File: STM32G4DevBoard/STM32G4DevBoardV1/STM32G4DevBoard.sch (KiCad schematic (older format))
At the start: 26 parts, among them J1 USB_B_Micro, J2 Conn_01x13, J3 Conn_01x13, U1 STM32G431KBTx, U2 LD3985M33R_SOT23, Y1 24MHz

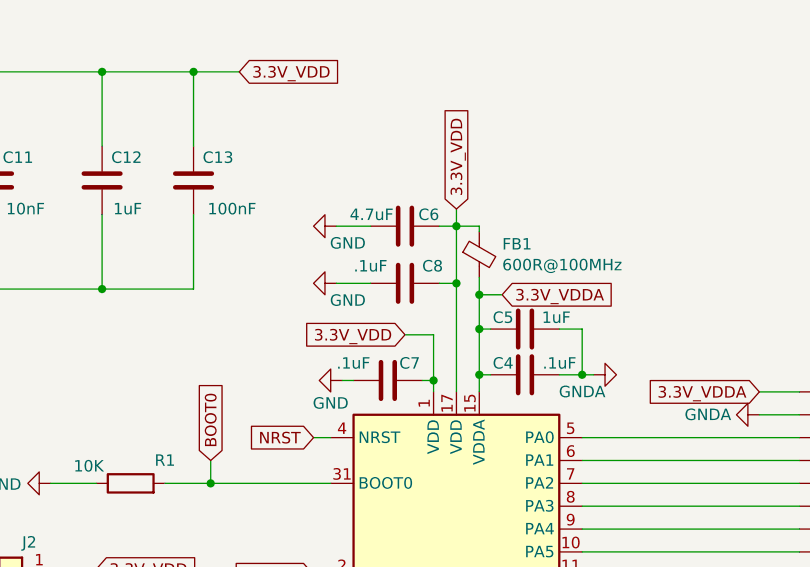
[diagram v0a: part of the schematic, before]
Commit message: Made plenty of Progress, finish routing power and a couple of pins
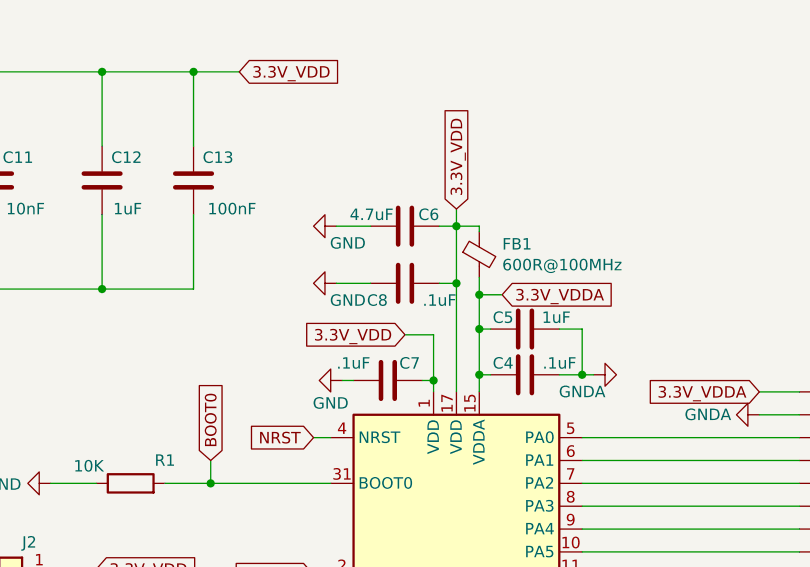
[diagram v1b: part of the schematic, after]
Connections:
- net 3.3V_VDD: now also C8.2; no longer C8.1
- net GND: now also C8.1; no longer C8.2
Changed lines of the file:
@@
 	6450 2900 6450 3100
-Wire Wire Line
-	6175 2675 6025 2675
 Wire Wire Line
 	6550 2675 6550 3150
@@
 F 3 "~" H 6325 2675 50  0001 C CNN
 	1    6325 2675
-	0    1    1    0
+	0    -1   -1   0
 $EndComp
 Wire Wire Line
@@
 Wire Wire Line
 	8050 4350 7900 4350
+Wire Wire Line
+	6175 2675 6025 2675
 $EndSCHEMATC

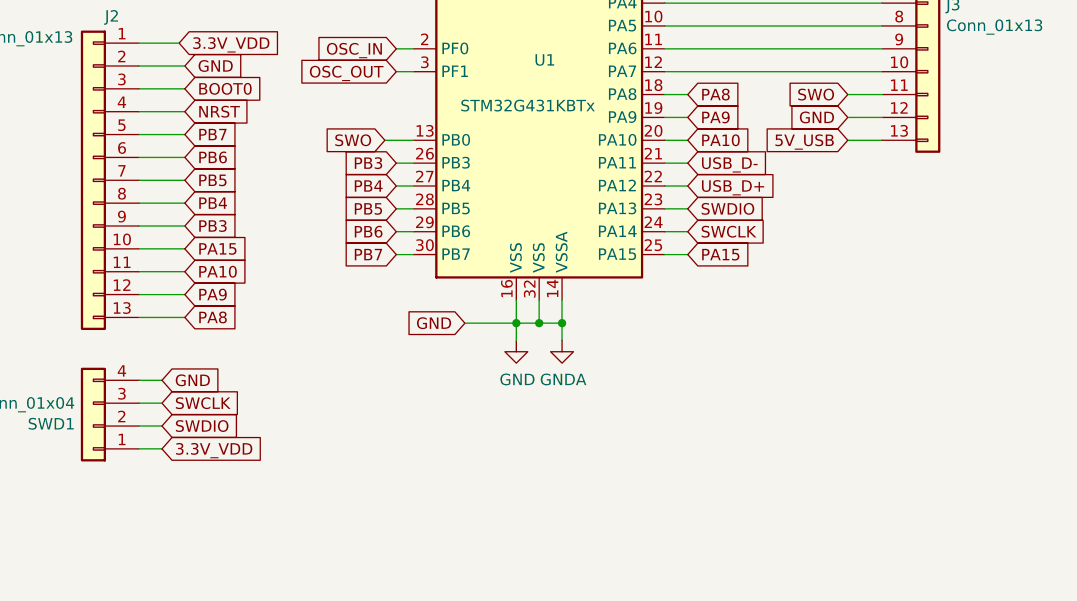
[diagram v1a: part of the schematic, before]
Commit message: Finish Power splitting and pin routing
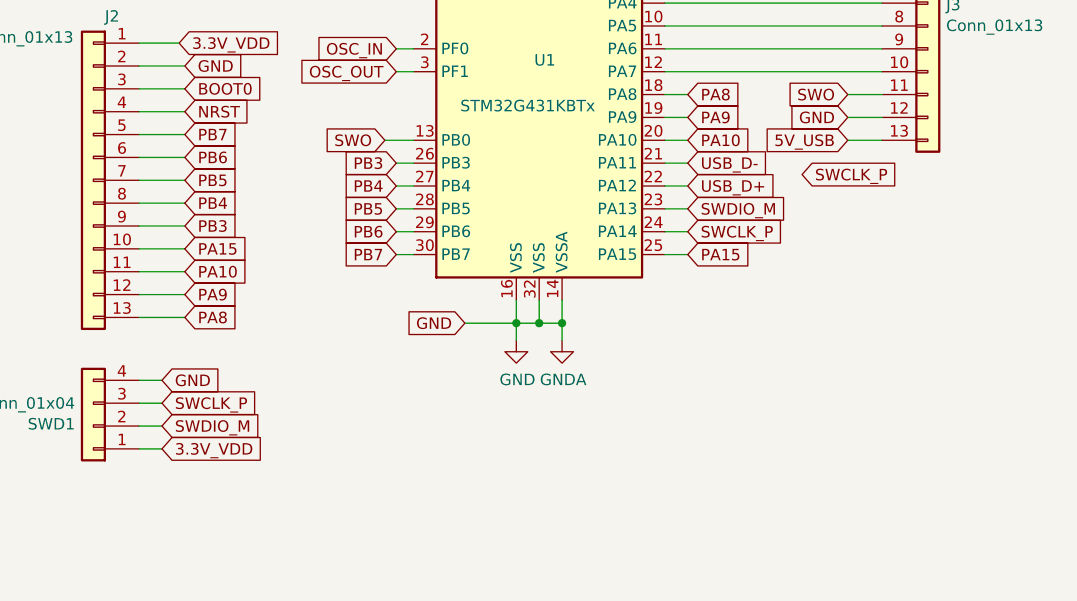
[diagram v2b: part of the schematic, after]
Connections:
- net SWCLK renamed SWCLK_P
- net SWDIO renamed SWDIO_M
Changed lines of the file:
@@
 Wire Wire Line
 	4800 5400 4900 5400
-Text GLabel 4900 5600 2    50   Input ~ 0
-SWDIO
 Wire Wire Line
 	4800 5600 4900 5600
-Text GLabel 4900 5500 2    50   Input ~ 0
-SWCLK
 Wire Wire Line
 	4900 5500 4800 5500
 Wire Wire Line
 	7200 4750 7100 4750
-Text GLabel 7200 4750 2    50   Input ~ 0
-SWCLK
 Wire Wire Line
 	7200 4650 7100 4650
-Text GLabel 7200 4650 2    50   Input ~ 0
-SWDIO
 Wire Wire Line
 	6450 5150 6225 5150
@@
 Wire Wire Line
 	6175 2675 6025 2675
+Text GLabel 4900 5500 2    50   Input ~ 0
+SWCLK_P
+Text GLabel 4900 5600 2    50   Input ~ 0
+SWDIO_M
+Text GLabel 7700 4500 2    50   Input ~ 0
+SWCLK_P
+Text GLabel 7200 4750 2    50   Input ~ 0
+SWCLK_P
+Text GLabel 7200 4650 2    50   Input ~ 0
+SWDIO_M
 $EndSCHEMATC

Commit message: Completed splitting ground plane and board routing
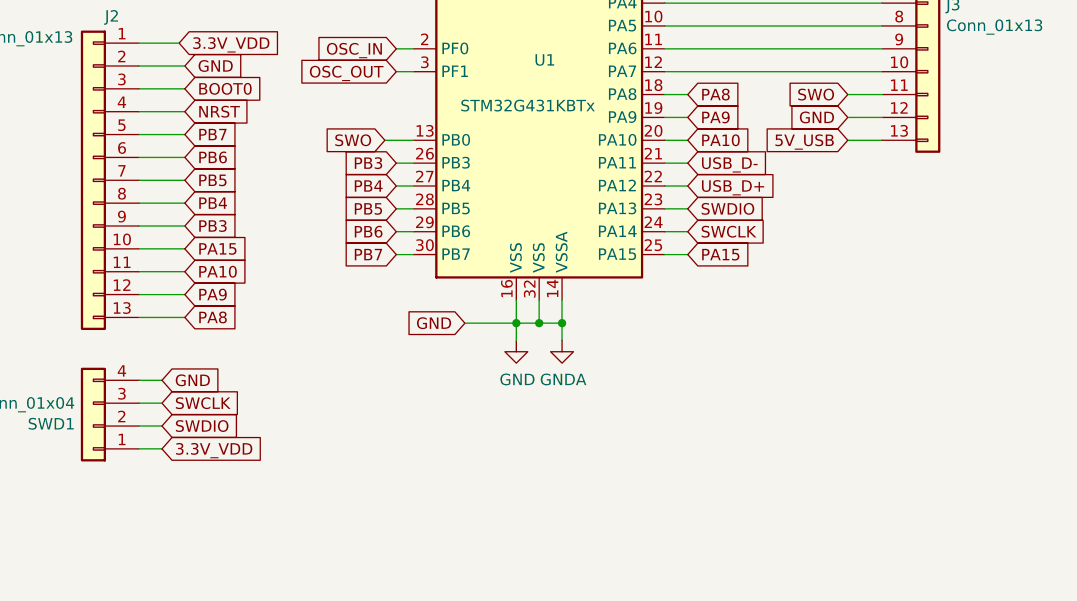
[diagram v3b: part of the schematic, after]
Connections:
- net SWCLK_P renamed SWCLK
- net SWDIO_M renamed SWDIO
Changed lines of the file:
@@
 Text GLabel 4900 5700 2    50   Input ~ 0
 3.3V_VDD
-Text GLabel 4900 5400 2    50   Input ~ 0
-GND
 Wire Wire Line
 	6650 2725 6650 2875
@@
 Text GLabel 7900 4350 0    50   Input ~ 0
 5V_USB
-Text GLabel 7900 4250 0    50   Input ~ 0
-GND
 Text GLabel 7200 4550 2    50   Input ~ 0
 USB_D+
@@
 	5000 5125 4800 5125
 Wire Wire Line
-	8050 4250 7900 4250
-Wire Wire Line
 	8050 3250 7875 3250
 Wire Wire Line
 	8050 3150 7875 3150
-Wire Wire Line
-	5000 4025 4800 4025
 Wire Wire Line
 	7100 4350 7200 4350
@@
 Wire Wire Line
 	5000 4125 4800 4125
-Text GLabel 5000 4025 2    50   Input ~ 0
-GND
 Wire Wire Line
 	6000 4350 5875 4350
@@
 	7200 4450 7100 4450
 Wire Wire Line
-	4800 5400 4900 5400
-Wire Wire Line
 	4800 5600 4900 5600
 Wire Wire Line
@@
 Wire Wire Line
 	7200 4650 7100 4650
-Wire Wire Line
-	6450 5150 6225 5150
-Text GLabel 6225 5150 0    50   Input ~ 0
-GND
 Wire Wire Line
 	4775 3550 4975 3550
@@
 	6175 2675 6025 2675
 Text GLabel 4900 5500 2    50   Input ~ 0
-SWCLK_P
+SWCLK
+Text GLabel 7200 4750 2    50   Input ~ 0
+SWCLK
+Text GLabel 7200 4650 2    50   Input ~ 0
+SWDIO
+Wire Wire Line
+	4800 5400 4900 5400
+Wire Wire Line
+	8050 4250 7900 4250
+Text GLabel 7900 4250 0    50   Input ~ 0
+GND
+Text GLabel 4900 5400 2    50   Input ~ 0
+GND
+Wire Wire Line
+	5000 4025 4800 4025
+Text GLabel 5000 4025 2    50   Input ~ 0
+GND
+Wire Wire Line
+	6450 5150 6225 5150
+Text GLabel 6225 5150 0    50   Input ~ 0
+GND
 Text GLabel 4900 5600 2    50   Input ~ 0
-SWDIO_M
-Text GLabel 7700 4500 2    50   Input ~ 0
-SWCLK_P
-Text GLabel 7200 4750 2    50   Input ~ 0
-SWCLK_P
-Text GLabel 7200 4650 2    50   Input ~ 0
-SWDIO_M
+SWDIO
 $EndSCHEMATC

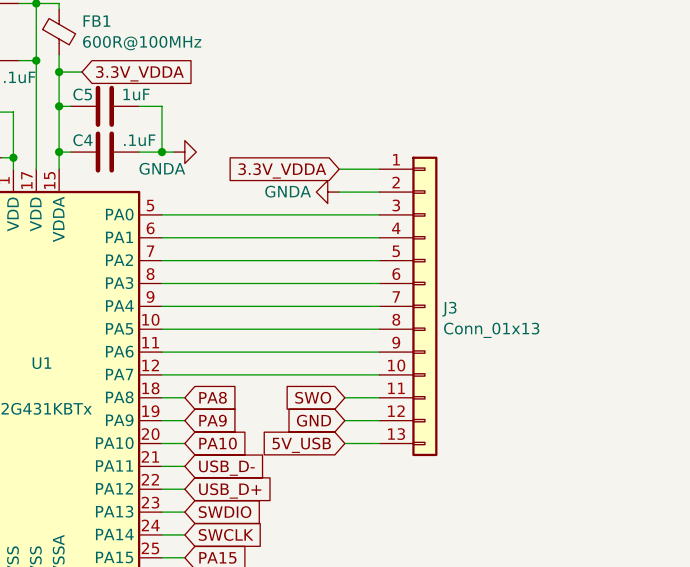
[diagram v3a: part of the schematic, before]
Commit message: Updated Silkscreen label for pins
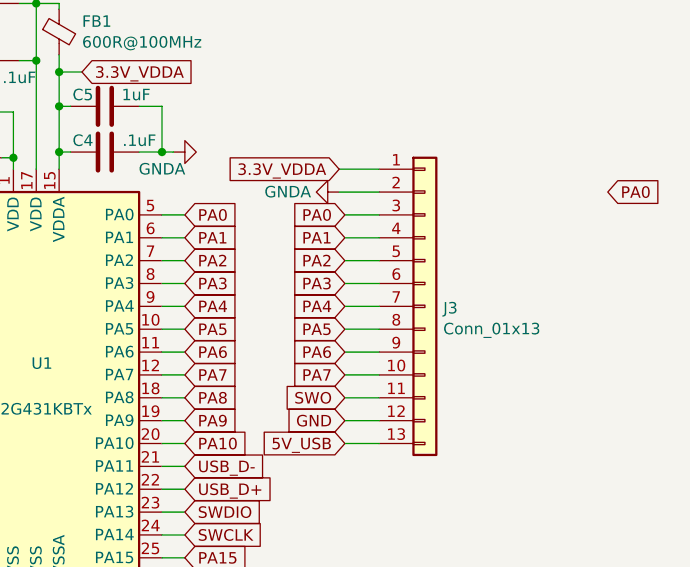
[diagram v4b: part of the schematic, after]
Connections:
- net PA5: now reaches J3.8 (Pin_8), U1.10 (PA5)
- net PA6: now reaches J3.9 (Pin_9), U1.11 (PA6)
- net PA7: now reaches J3.10 (Pin_10), U1.12 (PA7)
- net PA0: now reaches J3.3 (Pin_3), U1.5 (PA0)
- net PA1: now reaches J3.4 (Pin_4), U1.6 (PA1)
- net PA2: now reaches J3.5 (Pin_5), U1.7 (PA2)
- net PA3: now reaches J3.6 (Pin_6), U1.8 (PA3)
- net PA4: now reaches J3.7 (Pin_7), U1.9 (PA4)
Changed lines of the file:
@@
 	0    1    1    0
 $EndComp
-Wire Wire Line
-	7100 3350 8050 3350
 Text GLabel 4900 5700 2    50   Input ~ 0
 3.3V_VDD
@@
 SWO
 Wire Wire Line
-	7100 4050 8050 4050
-Wire Wire Line
-	7100 3950 8050 3950
-Wire Wire Line
-	7100 3850 8050 3850
-Wire Wire Line
-	7100 3750 8050 3750
-Wire Wire Line
-	7100 3650 8050 3650
-Wire Wire Line
-	7100 3550 8050 3550
-Wire Wire Line
-	7100 3450 8050 3450
-Wire Wire Line
 	7200 4550 7100 4550
 Wire Wire Line
@@
 Text GLabel 4900 5600 2    50   Input ~ 0
 SWDIO
+Text GLabel 9050 3250 2    50   Input ~ 0
+PA0
+Text GLabel 7900 3350 0    50   Input ~ 0
+PA0
+Wire Wire Line
+	8050 3350 7900 3350
+Wire Wire Line
+	7100 3350 7200 3350
+Text GLabel 7200 4050 2    50   Input ~ 0
+PA7
+Text GLabel 7200 3950 2    50   Input ~ 0
+PA6
+Text GLabel 7200 3850 2    50   Input ~ 0
+PA5
+Text GLabel 7200 3750 2    50   Input ~ 0
+PA4
+Text GLabel 7200 3650 2    50   Input ~ 0
+PA3
+Text GLabel 7200 3550 2    50   Input ~ 0
+PA2
+Text GLabel 7200 3450 2    50   Input ~ 0
+PA1
+Text GLabel 7200 3350 2    50   Input ~ 0
+PA0
+Text GLabel 7900 4050 0    50   Input ~ 0
+PA7
+Text GLabel 7900 3950 0    50   Input ~ 0
+PA6
+Text GLabel 7900 3850 0    50   Input ~ 0
+PA5
+Text GLabel 7900 3750 0    50   Input ~ 0
+PA4
+Text GLabel 7900 3650 0    50   Input ~ 0
+PA3
+Text GLabel 7900 3550 0    50   Input ~ 0
+PA2
+Text GLabel 7900 3450 0    50   Input ~ 0
+PA1
+Wire Wire Line
+	7200 3450 7100 3450
+Wire Wire Line
+	7100 3550 7200 3550
+Wire Wire Line
+	7100 4050 7200 4050
+Wire Wire Line
+	7200 3950 7100 3950
+Wire Wire Line
+	7100 3850 7200 3850
+Wire Wire Line
+	7200 3750 7100 3750
+Wire Wire Line
+	7200 3650 7100 3650
+Wire Wire Line
+	7900 3450 8050 3450
+Wire Wire Line
+	8050 3550 7900 3550
+Wire Wire Line
+	7900 3650 8050 3650
+Wire Wire Line
+	7900 3750 8050 3750
+Wire Wire Line
+	8050 3850 7900 3850
+Wire Wire Line
+	7900 3950 8050 3950
+Wire Wire Line
+	8050 4050 7900 4050
 $EndSCHEMATC
